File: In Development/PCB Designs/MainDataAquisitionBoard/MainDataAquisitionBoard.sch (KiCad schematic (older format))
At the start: 23 parts, among them J1 Conn_01x08, J10 3v3, J11 TopR, J12 TopL, J13 BottomR, J14 BottomL, J15 RTC, J16 XbeeL, J17 XbeeR, J18 Conn_02x03_Counter_Clockwise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

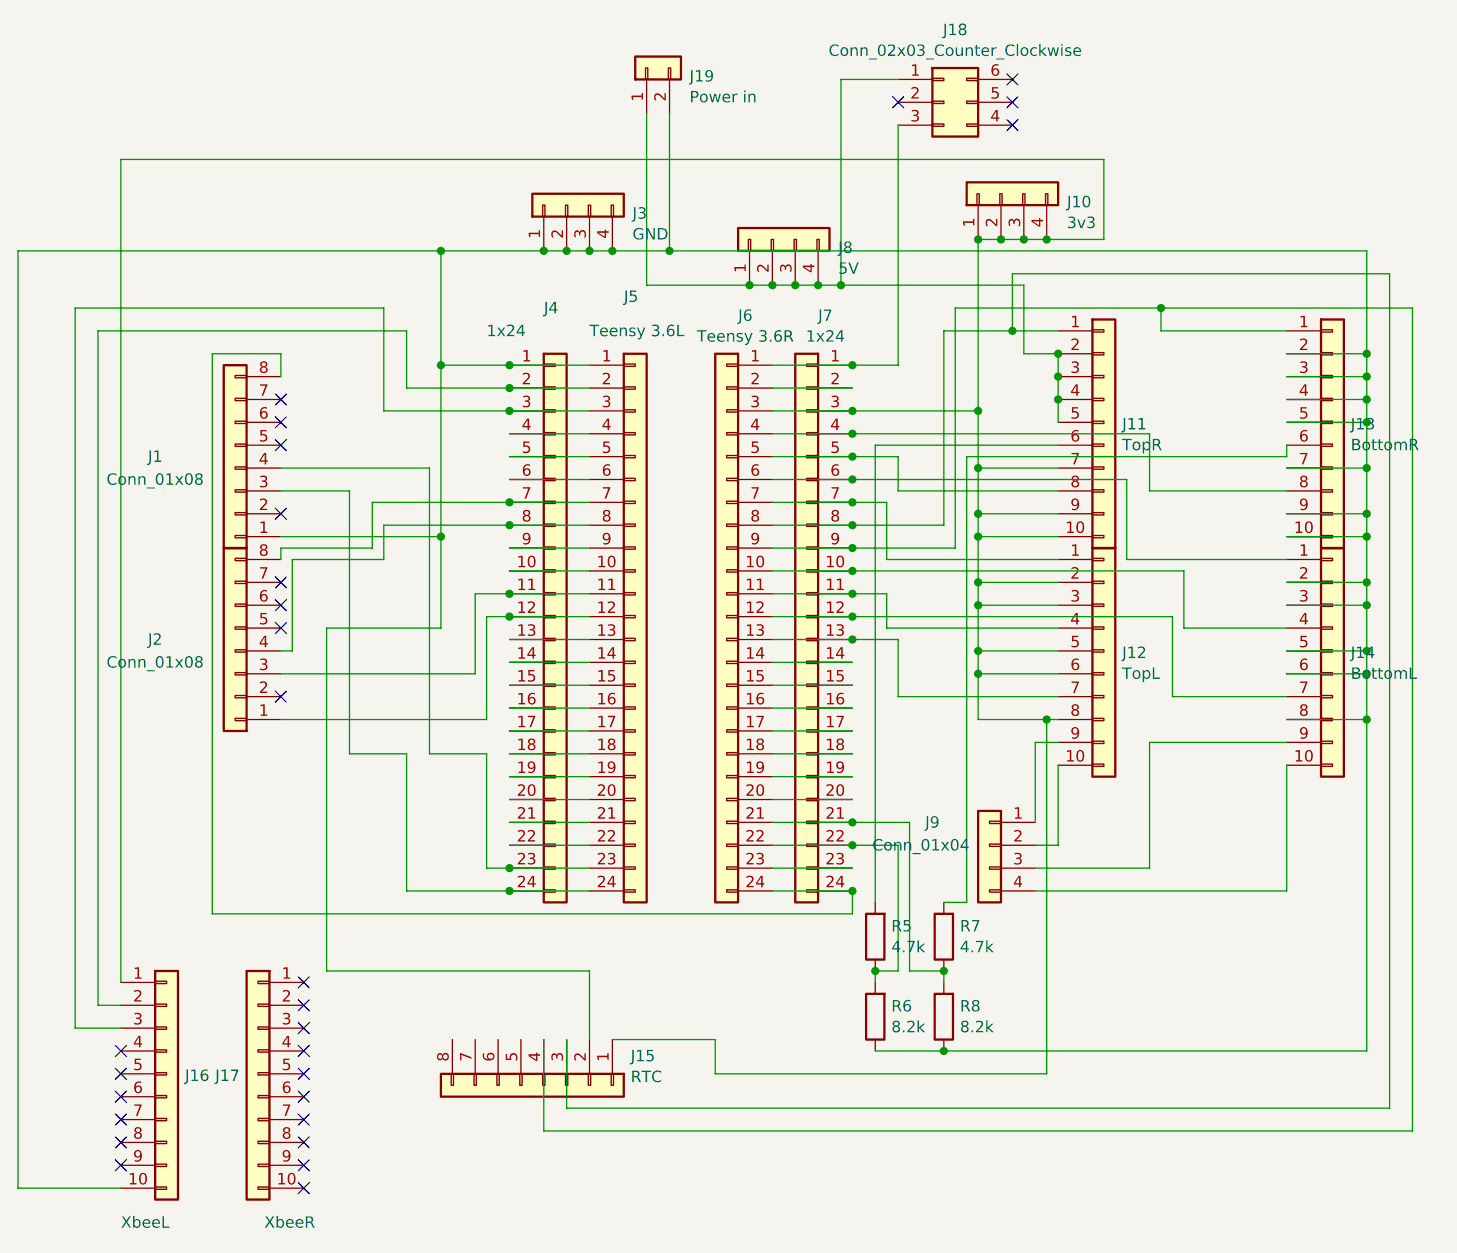
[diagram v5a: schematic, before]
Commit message: Finished DAQ and eCVT PCBs rev 2.1. Ready for ordering from JLCPCB
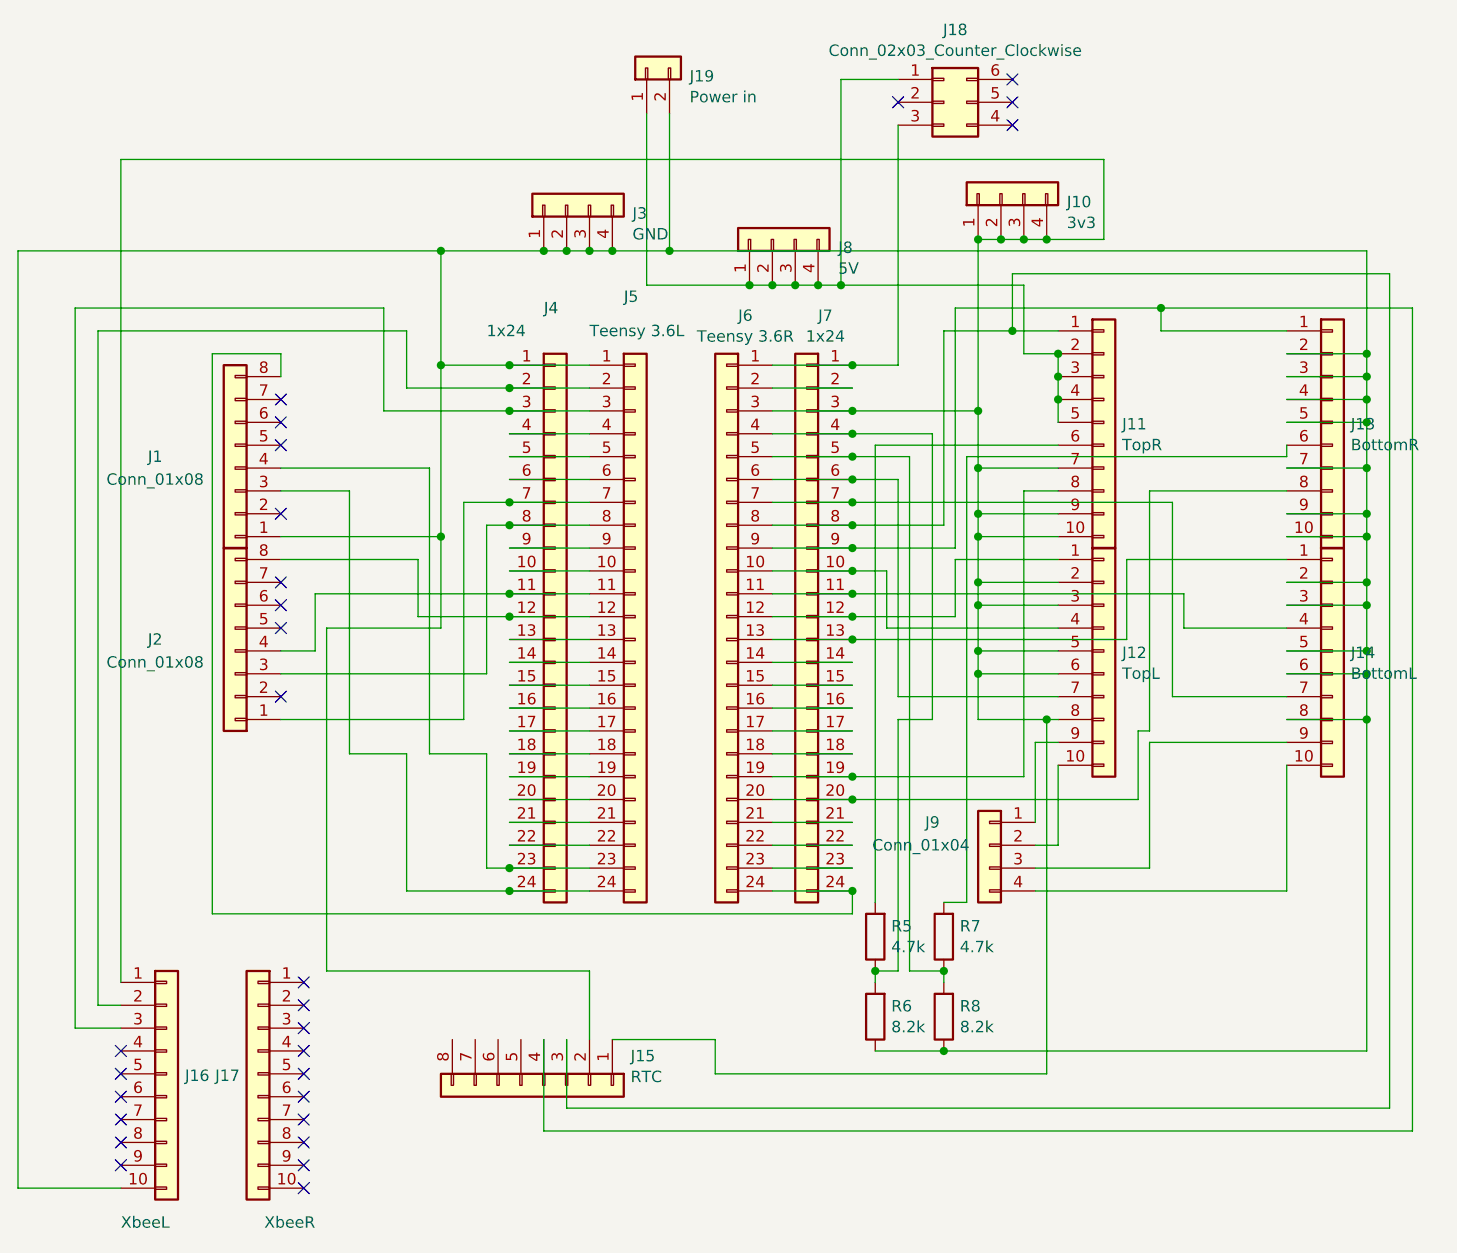
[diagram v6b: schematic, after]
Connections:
- net at J4.11 (Pin_11), J5.11 (Pin_11): now also J2.4 (Pin_4); no longer J2.3 (Pin_3)
- net at J4.12 (Pin_12), J5.12 (Pin_12): now also J2.8 (Pin_8); no longer J2.1 (Pin_1)
- net at J4.7 (Pin_7), J5.7 (Pin_7): now also J2.1 (Pin_1); no longer J2.8 (Pin_8)
- net at J4.8 (Pin_8), J5.8 (Pin_8): now also J2.3 (Pin_3); no longer J2.4 (Pin_4)
- net at J6.10 (Pin_10), J7.10 (Pin_10): now also J12.4 (Pin_4); no longer J14.4 (Pin_4)
- net at J6.11 (Pin_11), J7.11 (Pin_11): now also J14.4 (Pin_4); no longer J12.4 (Pin_4)
- net at J6.12 (Pin_12), J7.12 (Pin_12): now also J12.1 (Pin_1); no longer J14.7 (Pin_7)
- net at J6.13 (Pin_13), J7.13 (Pin_13): now also J14.1 (Pin_1); no longer J12.7 (Pin_7)
- net at J6.19 (Pin_19), J7.19 (Pin_19): now also J11.8 (Pin_8)
- net at J6.20 (Pin_20), J7.20 (Pin_20): now also J13.8 (Pin_8)
- net at J6.21 (Pin_21), J7.21 (Pin_21): no longer R7.1, R8.2
- net at J6.22 (Pin_22), J7.22 (Pin_22): no longer R5.1, R6.2
- net at J6.4 (Pin_4), J7.4 (Pin_4): now also R5.1, R6.2; no longer J13.8 (Pin_8)
- net at J6.5 (Pin_5), J7.5 (Pin_5): now also R7.1, R8.2; no longer J11.8 (Pin_8)
- net at J6.6 (Pin_6), J7.6 (Pin_6): now also J12.7 (Pin_7); no longer J14.1 (Pin_1)
- net at J6.7 (Pin_7), J7.7 (Pin_7): now also J14.7 (Pin_7); no longer J12.1 (Pin_1)
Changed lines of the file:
@@
 Connection ~ 4450 2950
-Wire Wire Line
-	3900 3800 3900 3650
-Wire Wire Line
-	3900 3650 4450 3650
-Connection ~ 4450 3650
-Wire Wire Line
-	3850 3550 4450 3550
-Connection ~ 4450 3550
 Wire Wire Line
 	4350 4650 4350 5150
@@
 	6850 2800 6650 2800
 Wire Wire Line
-	6350 2800 6350 3650
-Wire Wire Line
 	5600 3650 5950 3650
-Connection ~ 5950 3650
-Wire Wire Line
-	5950 3650 6350 3650
 Wire Wire Line
 	7850 2800 7300 2800
@@
 Wire Wire Line
 	7300 2700 6400 2700
-Wire Wire Line
-	6400 2700 6400 3750
-Wire Wire Line
-	6400 3750 5950 3750
-Connection ~ 5950 3750
 Wire Wire Line
 	4150 2950 4150 2450
@@
 	7850 4400 7350 4400
 Wire Wire Line
-	7350 4400 7350 4050
-Wire Wire Line
-	7350 4050 5950 4050
-Connection ~ 5950 4050
-Wire Wire Line
 	6850 4100 6100 4100
 Wire Wire Line
-	6100 4100 6100 3950
-Wire Wire Line
-	6100 3950 5950 3950
-Connection ~ 5950 3950
-Wire Wire Line
 	7850 4100 7400 4100
 Wire Wire Line
-	7400 4100 7400 3850
-Wire Wire Line
-	7400 3850 5950 3850
-Connection ~ 5950 3850
-Wire Wire Line
 	6050 5650 6050 5600
 Wire Wire Line
@@
 Wire Wire Line
 	6050 5600 6150 5600
-Wire Wire Line
-	6150 5600 6150 5050
-Wire Wire Line
-	6150 5050 5950 5050
 Connection ~ 6050 5600
-Connection ~ 5950 5050
 Wire Wire Line
 	6350 5600 6200 5600
-Wire Wire Line
-	6200 5600 6200 4950
-Wire Wire Line
-	6200 4950 5950 4950
 Connection ~ 6350 5600
-Connection ~ 5950 4950
 Wire Wire Line
 	8200 4500 8200 5950
@@
 	6450 5300 6350 5300
 Wire Wire Line
-	6850 3800 6100 3800
-Wire Wire Line
-	6100 3800 6100 3550
-Wire Wire Line
-	6100 3550 5950 3550
-Connection ~ 5950 3550
-Wire Wire Line
 	7850 3800 7150 3800
-Wire Wire Line
-	7150 3800 7150 3450
-Wire Wire Line
-	7150 3450 5950 3450
-Connection ~ 5950 3450
-Wire Wire Line
-	6850 3500 6150 3500
-Wire Wire Line
-	6150 3500 6150 3350
-Wire Wire Line
-	6150 3350 5950 3350
-Connection ~ 5950 3350
 Wire Wire Line
 	3150 5350 5950 5350
@@
 Wire Wire Line
 	7850 3500 7250 3500
-Wire Wire Line
-	7250 3500 7250 3250
-Wire Wire Line
-	7250 3250 5950 3250
-Connection ~ 5950 3250
 $Comp
 L Connector_Generic:Conn_01x04 J3
@@
 	3750 3500 3450 3500
 Wire Wire Line
-	3500 3800 3500 4200
-Wire Wire Line
-	3500 4200 3450 4200
-Wire Wire Line
-	3450 3750 3450 3800
-Wire Wire Line
-	3850 3550 3850 3750
-Wire Wire Line
-	3450 3750 3850 3750
-Wire Wire Line
 	6050 3300 6050 5300
 Wire Wire Line
-	5950 4150 6150 4150
-Wire Wire Line
-	6150 4150 6150 4400
-Wire Wire Line
 	6150 4400 6850 4400
-Connection ~ 5950 4150
 $Comp
 L Connector_Generic:Conn_01x08 J15
@@
 Connection ~ 4150 2950
 Wire Wire Line
-	3500 3800 3900 3800
-Wire Wire Line
 	3650 4100 3650 5600
 Wire Wire Line
@@
 Wire Wire Line
 	4150 3700 4150 4100
-Wire Wire Line
-	3450 4300 4300 4300
-Wire Wire Line
-	4300 4300 4300 3950
-Wire Wire Line
-	4300 3950 4450 3950
-Connection ~ 4450 3950
-Wire Wire Line
-	3450 4500 4350 4500
-Wire Wire Line
-	4350 4500 4350 4050
-Wire Wire Line
-	4350 4050 4450 4050
-Connection ~ 4450 4050
 $Comp
 L Connector_Generic:Conn_01x02 J19
@@
 Wire Wire Line
 	5150 2450 8200 2450
+Wire Wire Line
+	4450 3950 3600 3950
+Wire Wire Line
+	3600 3950 3600 4200
+Wire Wire Line
+	3600 4200 3450 4200
+Connection ~ 4450 3950
+Wire Wire Line
+	4450 4050 4050 4050
+Wire Wire Line
+	4050 4050 4050 3800
+Wire Wire Line
+	4050 3800 3450 3800
+Connection ~ 4450 4050
+Wire Wire Line
+	4450 3650 4350 3650
+Connection ~ 4450 3650
+Wire Wire Line
+	4450 3550 4250 3550
+Connection ~ 4450 3550
+Wire Wire Line
+	4250 4500 3450 4500
+Wire Wire Line
+	4250 3550 4250 4500
+Wire Wire Line
+	4350 3650 4350 4300
+Wire Wire Line
+	4350 4300 3450 4300
+Wire Wire Line
+	6150 4500 6300 4500
+Wire Wire Line
+	6300 4500 6300 3250
+Wire Wire Line
+	6300 3250 5950 3250
+Wire Wire Line
+	6150 4500 6150 5600
+Connection ~ 5950 3250
+Wire Wire Line
+	6200 3350 6200 5600
+Wire Wire Line
+	7250 3500 7250 4550
+Wire Wire Line
+	7250 4550 7200 4550
+Wire Wire Line
+	7200 4550 7200 4850
+Wire Wire Line
+	7200 4850 5950 4850
+Connection ~ 5950 4850
+Wire Wire Line
+	6850 3500 6700 3500
+Wire Wire Line
+	6700 3500 6700 4750
+Wire Wire Line
+	6700 4750 5950 4750
+Connection ~ 5950 4750
+Connection ~ 5950 3350
+Wire Wire Line
+	6200 3350 5950 3350
+Wire Wire Line
+	6850 3800 6400 3800
+Wire Wire Line
+	6400 3800 6400 4050
+Wire Wire Line
+	6400 4050 5950 4050
+Connection ~ 5950 4050
+Wire Wire Line
+	7150 4150 5950 4150
+Wire Wire Line
+	7150 3800 7150 4150
+Connection ~ 5950 4150
+Wire Wire Line
+	6100 3850 5950 3850
+Wire Wire Line
+	6100 3850 6100 4100
+Connection ~ 5950 3850
+Wire Wire Line
+	7400 4100 7400 3950
+Wire Wire Line
+	7400 3950 5950 3950
+Connection ~ 5950 3950
+Wire Wire Line
+	6400 2700 6400 3750
+Wire Wire Line
+	6350 2800 6350 3650
+Connection ~ 5950 3650
+Wire Wire Line
+	5950 3650 6350 3650
+Connection ~ 5950 3750
+Wire Wire Line
+	6400 3750 5950 3750
+Wire Wire Line
+	6150 3450 5950 3450
+Wire Wire Line
+	6150 3450 6150 4400
+Connection ~ 5950 3450
+Wire Wire Line
+	7350 4400 7350 3550
+Wire Wire Line
+	7350 3550 5950 3550
+Connection ~ 5950 3550
 $EndSCHEMATC
